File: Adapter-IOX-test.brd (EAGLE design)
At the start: 63.5 x 25.4 mm, 51 parts, among them Q0 P-FET, Q1 P-FET, Q10 P-FET, Q11 P-FET, Q12 P-FET, Q13 P-FET, Q14 P-FET, Q15 P-FET, Q2 P-FET, Q3 P-FET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

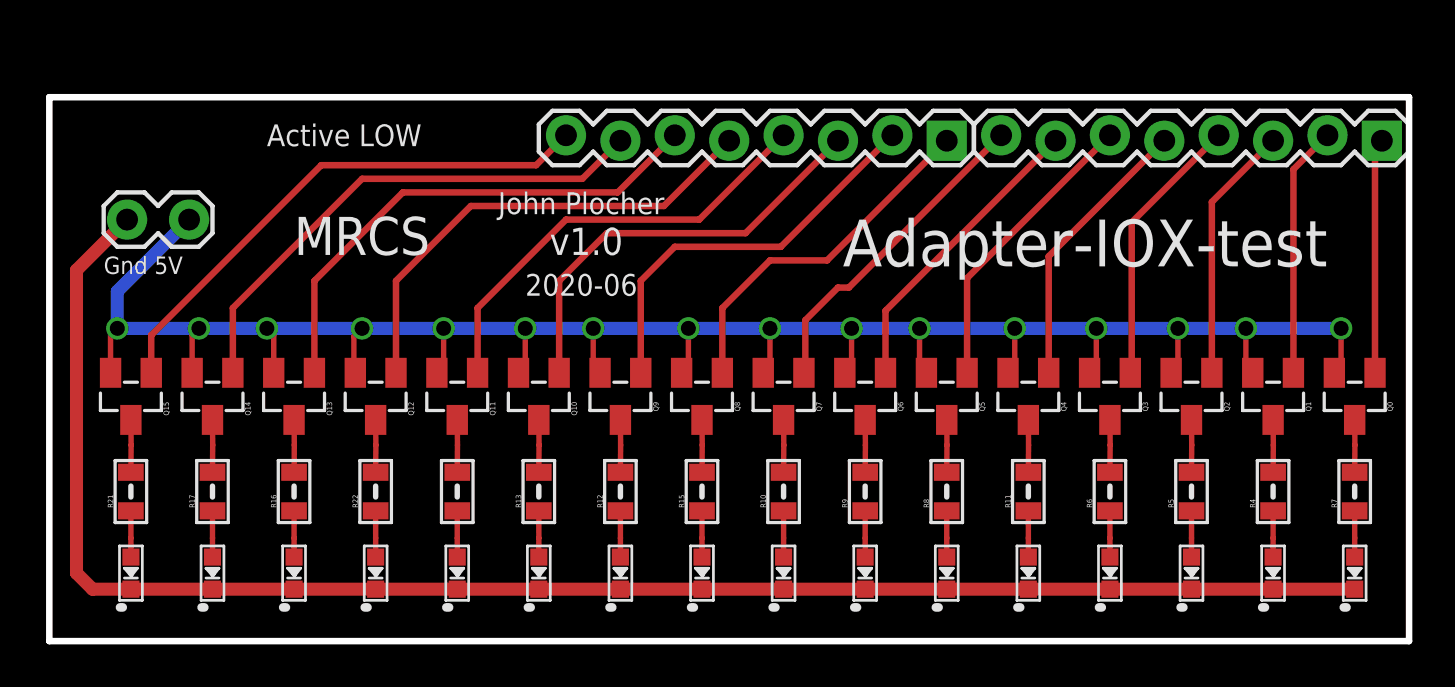
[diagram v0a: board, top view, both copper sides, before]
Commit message: higher density, narrow the board so 2x work with IOX-32
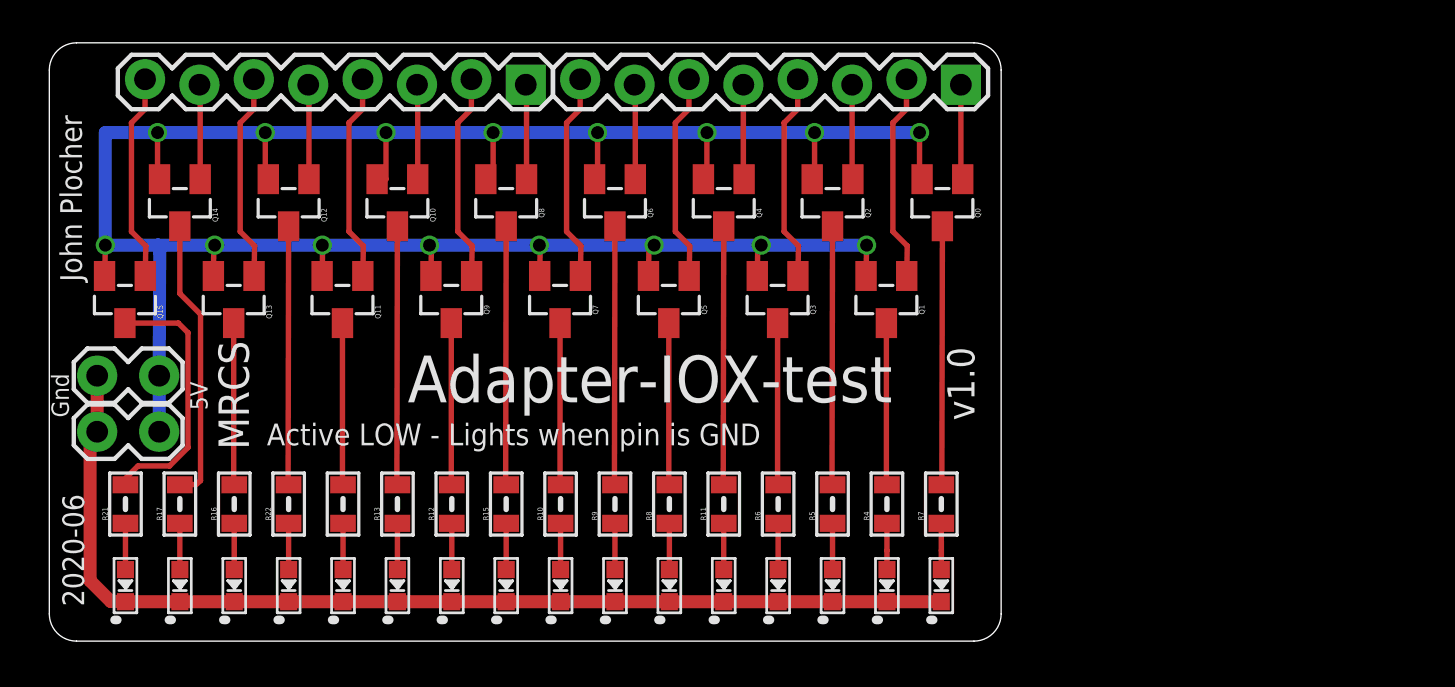
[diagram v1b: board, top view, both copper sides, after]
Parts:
- added CON2: (no value), SPCoast:1X02_LOCK
- moved Q0 21.3 mm to (41.7, 20.5)
- moved J1 19.8 mm to (42.6, 26.1)
- moved J2 19.8 mm to (22.3, 26.1)
- moved LED1 19.3 mm to (41.7, 2.59)
- moved R7 19.3 mm to (41.7, 6.40)
- moved Q2 19.0 mm to (36.6, 20.5)
- moved Q1 18.6 mm to (39.1, 16.0)
- moved LED2 18.0 mm to (39.1, 2.59)
- moved R4 18.0 mm to (39.1, 6.40)
- moved Q4 16.9 mm to (31.5, 20.5)
- moved LED3 16.8 mm to (36.6, 2.59)
- moved R5 16.8 mm to (36.6, 6.40)
- moved Q3 16.2 mm to (34.0, 16.0)
- moved LED4 15.5 mm to (34.0, 2.59)
- moved R6 15.5 mm to (34.0, 6.40)
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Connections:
- net GND: now also CON2.1
- net VCC: now also CON2.2
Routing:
- net GND: track 77.5 -> 50.0 mm
- net P15: track 24.4 -> 4.45 mm
- net P13: track 22.6 -> 4.45 mm
- net P11: track 20.0 -> 4.45 mm
- net P16: track 25.1 -> 9.73 mm
- net P14: track 23.9 -> 9.73 mm
- net P9: track 16.7 -> 4.45 mm
- net P12: track 21.5 -> 9.73 mm
- net N$30: track 2.45 -> 13.3 mm
- net N$31: track 2.45 -> 12.3 mm
- net P7: track 14.1 -> 4.45 mm
- net N$4: track 2.45 -> 12.1 mm
- net N$12: track 2.45 -> 12.1 mm
- net N$28: track 2.45 -> 12.1 mm
- net N$46: track 2.45 -> 12.1 mm
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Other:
- board size 63.5 x 25.4 mm -> 44.5 x 27.9 mm
- board text added: "5V"
- board text added: "5V GND"
- board text added: "Active LOW - Lights when pin is GND"
- board text added: "Gnd"
- board text removed: "Active LOW"
- board text removed: "Gnd 5V"

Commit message: fixed SPCoast lbr part orientation
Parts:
- turned LED1 to 90 degrees
- turned LED10 to 90 degrees
- turned LED11 to 90 degrees
- turned LED12 to 90 degrees
- turned LED13 to 90 degrees
- turned LED14 to 90 degrees
- turned LED15 to 90 degrees
- turned LED16 to 90 degrees
- turned LED2 to 90 degrees
- turned LED3 to 90 degrees
- turned LED4 to 90 degrees
- turned LED5 to 90 degrees
- turned LED6 to 90 degrees
- turned LED7 to 90 degrees
- turned LED8 to 90 degrees
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
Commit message: added values for connectors
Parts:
- CON1, CON2, J1, J2: value (none) -> 0.100
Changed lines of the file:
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@@
 <attribute name="NAME" x="2.7305" y="5.6388" size="0.254" layer="25" rot="R90"/>
 </element>
-<element name="J1" library="SPCoast" package="1X08_LOCK" value="" x="42.5704" y="26.1112" smashed="yes" rot="R180">
+<element name="J1" library="SPCoast" package="1X08_LOCK" value="0.100" x="42.5704" y="26.1112" smashed="yes" rot="R180">
 <attribute name="VALUE" x="43.8404" y="29.2862" size="1.27" layer="27" rot="R180"/>
 </element>
-<element name="J2" library="SPCoast" package="1X08_LOCK" value="" x="22.2504" y="26.1112" smashed="yes" rot="R180">
+<element name="J2" library="SPCoast" package="1X08_LOCK" value="0.100" x="22.2504" y="26.1112" smashed="yes" rot="R180">
 <attribute name="VALUE" x="23.5204" y="29.2862" size="1.27" layer="27" rot="R180"/>
 </element>
-<element name="CON1" library="SPCoast" package="1X02_LOCK" value="" x="2.413" y="12.3952" smashed="yes">
+<element name="CON1" library="SPCoast" package="1X02_LOCK" value="0.100" x="2.413" y="12.3952" smashed="yes">
 <attribute name="VALUE" x="1.143" y="9.2202" size="1.27" layer="27"/>
 </element>
-<element name="CON2" library="SPCoast" package="1X02_LOCK" value="" x="2.413" y="9.779" smashed="yes">
+<element name="CON2" library="SPCoast" package="1X02_LOCK" value="0.100" x="2.413" y="9.779" smashed="yes">
 <attribute name="VALUE" x="1.143" y="6.604" size="1.27" layer="27"/>
 </element>
